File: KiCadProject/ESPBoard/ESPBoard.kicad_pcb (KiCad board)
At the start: 6 copper layers, 44.9 x 42.5 mm, 77 parts, among them J201 Conn_02x05, J202 Conn_01x02, J203 Conn_02x05, J204 JST_SM04B, J205 DNP, J206 1x05 female, J207 JST_SM04B, Q401 NFET_Gatenames, Q402 PMOS_Gatenames, Q403 NFET_Gatenames, Q404 PMOS_Gatenames, Q405 NFET_Gatenames, Q406 PMOS_Gatenames, Q407 NFET_Gatenames, Q408 PMOS_Gatenames, SW301 SW_Push, SW302 SW_Push, U301 ESP32-S3-WROOM-1

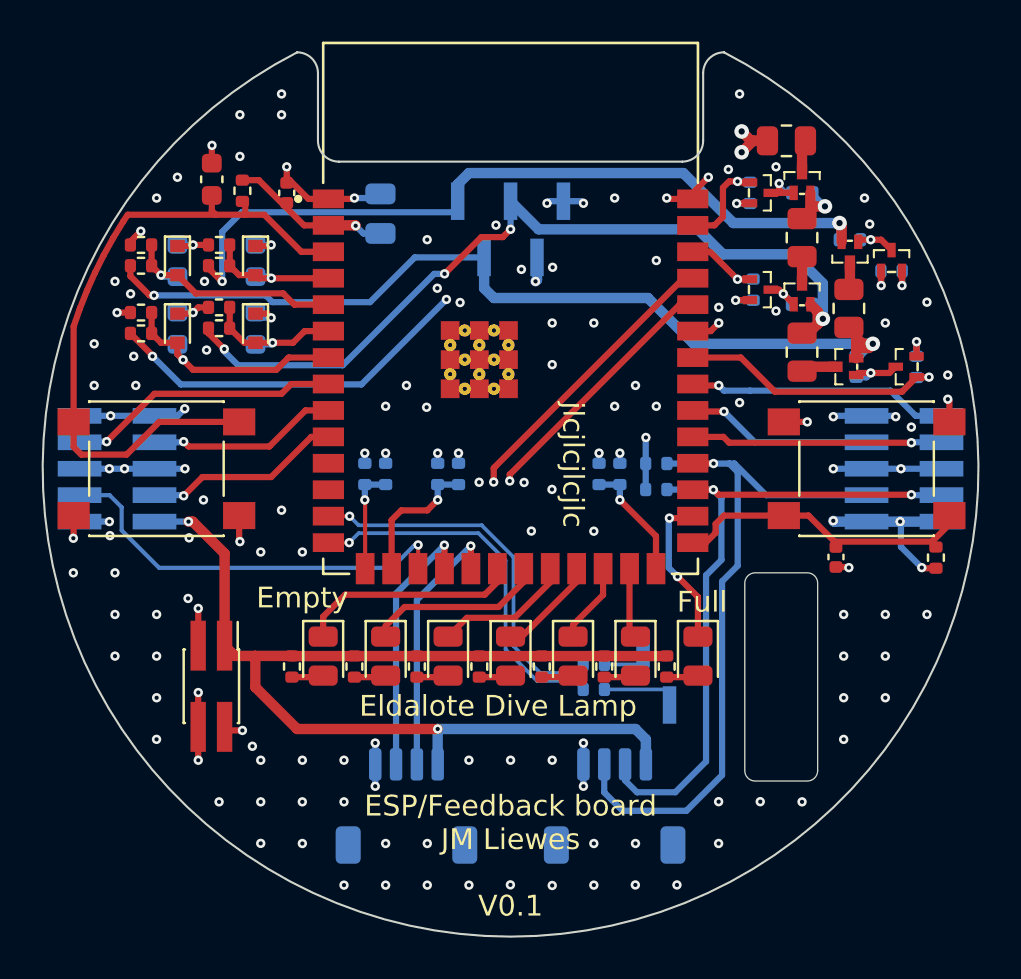
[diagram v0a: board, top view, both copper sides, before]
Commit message: Made ready to order PCBs. Some problems with ordering due to misunderstanding. Thinking about solutions
Signed-off-by: Eldalote.Electronics <Eldalote.Electronics@gmail.com>
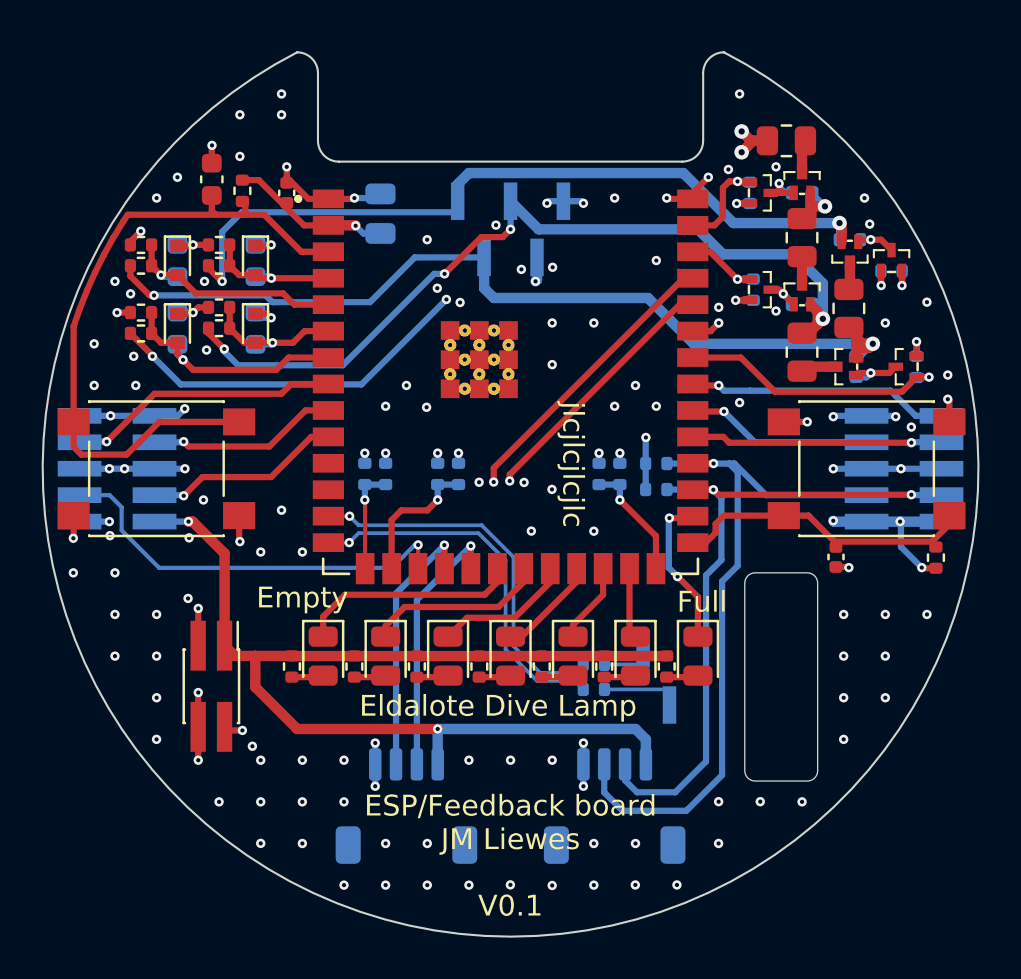
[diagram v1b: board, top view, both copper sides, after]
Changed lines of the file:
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@@
       (layerselection 0x00010fc_ffffffff)
       (disableapertmacros false)
-      (usegerberextensions false)
+      (usegerberextensions true)
       (usegerberattributes true)
       (usegerberadvancedattributes true)
@@
       (plotinvisibletext false)
       (sketchpadsonfab false)
-      (subtractmaskfromsilk false)
+      (subtractmaskfromsilk true)
       (outputformat 1)
       (mirror false)
-      (drillshape 1)
+      (drillshape 0)
       (scaleselection 1)
-      (outputdirectory "")
+      (outputdirectory "Fab/")
     )
   )
@@
     (fp_line (start -1 -0.625) (end 1 -0.625) (layer "F.Fab") (width 0.1))
     (fp_line (start 1 0.625) (end -1 0.625) (layer "F.Fab") (width 0.1))
-    (pad "1" smd roundrect (at -0.9125 0 270) (size 1.025 1.4) (layers "F.Cu" "F.Paste" "F.Mask") (roundrect_rratio 0.243902)
+    (pad "1" smd roundrect (at -0.9125 0 270) (size 1.025 1.4) (layers "F.Cu" "F.Paste" "F.Mask") (roundrect_rratio 0.243902439)
       (net 57 "/P4 Batsense-Balancing/C4L") (pintype "passive"))
-    (pad "2" smd roundrect (at 0.9125 0 270) (size 1.025 1.4) (layers "F.Cu" "F.Paste" "F.Mask") (roundrect_rratio 0.243902)
+    (pad "2" smd roundrect (at 0.9125 0 270) (size 1.025 1.4) (layers "F.Cu" "F.Paste" "F.Mask") (roundrect_rratio 0.243902439)
       (net 40 "Cell3") (pintype "passive"))
     (model "${KICAD6_3DMODEL_DIR}/Resistor_SMD.3dshapes/R_0805_2012Metric.wrl"
@@
     (fp_line (start 1 0.625) (end -1 0.625) (layer "F.Fab") (width 0.1))
     (fp_line (start -1 -0.625) (end 1 -0.625) (layer "F.Fab") (width 0.1))
-    (pad "1" smd roundrect (at -0.9125 0 90) (size 1.025 1.4) (layers "F.Cu" "F.Paste" "F.Mask") (roundrect_rratio 0.243902)
+    (pad "1" smd roundrect (at -0.9125 0 90) (size 1.025 1.4) (layers "F.Cu" "F.Paste" "F.Mask") (roundrect_rratio 0.243902439)
       (net 58 "/P4 Batsense-Balancing/C3L") (pintype "passive"))
-    (pad "2" smd roundrect (at 0.9125 0 90) (size 1.025 1.4) (layers "F.Cu" "F.Paste" "F.Mask") (roundrect_rratio 0.243902)
+    (pad "2" smd roundrect (at 0.9125 0 90) (size 1.025 1.4) (layers "F.Cu" "F.Paste" "F.Mask") (roundrect_rratio 0.243902439)
       (net 41 "Cell2") (pintype "passive"))
     (model "${KICAD6_3DMODEL_DIR}/Resistor_SMD.3dshapes/R_0805_2012Metric.wrl"
@@
       (effects (font (size 1 1) (thickness 0.15)))
     )
-    (fp_line (start -9 -12.75) (end 9 -12.75) (layer "F.SilkS") (width 0.127))
     (fp_line (start -9 12.02) (end -9 12.75) (layer "F.SilkS") (width 0.127))
-    (fp_line (start 9 -12.75) (end 9 -6.03) (layer "F.SilkS") (width 0.127))
     (fp_line (start 9 12.02) (end 9 12.75) (layer "F.SilkS") (width 0.127))
     (fp_line (start 9 12.75) (end 7.755 12.75) (layer "F.SilkS") (width 0.127))
     (fp_line (start -9 12.75) (end -7.755 12.75) (layer "F.SilkS") (width 0.127))
-    (fp_line (start -9 -6.03) (end -9 -12.75) (layer "F.SilkS") (width 0.127))
     (fp_circle (center -10.2 -5.26) (end -10.1 -5.26) (layer "F.SilkS") (width 0.2) (fill none))
     (fp_line (start -9.75 13.5) (end -9.75 -13) (layer "F.CrtYd") (width 0.05))
@@
     (fp_line (start 1 0.625) (end -1 0.625) (layer "F.Fab") (width 0.1))
     (fp_line (start -1 -0.625) (end 1 -0.625) (layer "F.Fab") (width 0.1))
-    (pad "1" smd roundrect (at -0.9125 0 180) (size 1.025 1.4) (layers "F.Cu" "F.Paste" "F.Mask") (roundrect_rratio 0.243902)
+    (pad "1" smd roundrect (at -0.9125 0 180) (size 1.025 1.4) (layers "F.Cu" "F.Paste" "F.Mask") (roundrect_rratio 0.243902439)
       (net 60 "/P4 Batsense-Balancing/C1L") (pintype "passive"))
-    (pad "2" smd roundrect (at 0.9125 0 180) (size 1.025 1.4) (layers "F.Cu" "F.Paste" "F.Mask") (roundrect_rratio 0.243902)
+    (pad "2" smd roundrect (at 0.9125 0 180) (size 1.025 1.4) (layers "F.Cu" "F.Paste" "F.Mask") (roundrect_rratio 0.243902439)
       (net 21 "GND") (pintype "passive"))
     (model "${KICAD6_3DMODEL_DIR}/Resistor_SMD.3dshapes/R_0805_2012Metric.wrl"
@@
     (fp_line (start 1 0.625) (end -1 0.625) (layer "F.Fab") (width 0.1))
     (fp_line (start -1 -0.625) (end 1 -0.625) (layer "F.Fab") (width 0.1))
-    (pad "1" smd roundrect (at -0.9125 0 90) (size 1.025 1.4) (layers "F.Cu" "F.Paste" "F.Mask") (roundrect_rratio 0.243902)
+    (pad "1" smd roundrect (at -0.9125 0 90) (size 1.025 1.4) (layers "F.Cu" "F.Paste" "F.Mask") (roundrect_rratio 0.243902439)
       (net 59 "/P4 Batsense-Balancing/C2L") (pintype "passive"))
-    (pad "2" smd roundrect (at 0.9125 0 90) (size 1.025 1.4) (layers "F.Cu" "F.Paste" "F.Mask") (roundrect_rratio 0.243902)
+    (pad "2" smd roundrect (at 0.9125 0 90) (size 1.025 1.4) (layers "F.Cu" "F.Paste" "F.Mask") (roundrect_rratio 0.243902439)
       (net 42 "Cell1") (pintype "passive"))
     (model "${KICAD6_3DMODEL_DIR}/Resistor_SMD.3dshapes/R_0805_2012Metric.wrl"
@@
     (pad "4" smd roundrect (at 1.5 2 180) (size 0.6 1.55) (layers "B.Cu" "B.Paste" "B.Mask") (roundrect_rratio 0.25)
       (net 21 "GND") (pinfunction "Pin_4") (pintype "passive"))
-    (pad "MP" smd roundrect (at -2.8 -1.875 180) (size 1.2 1.8) (layers "B.Cu" "B.Paste" "B.Mask") (roundrect_rratio 0.208333))
-    (pad "MP" smd roundrect (at 2.8 -1.875 180) (size 1.2 1.8) (layers "B.Cu" "B.Paste" "B.Mask") (roundrect_rratio 0.208333))
+    (pad "MP" smd roundrect (at -2.8 -1.875 180) (size 1.2 1.8) (layers "B.Cu" "B.Paste" "B.Mask") (roundrect_rratio 0.2083333333))
+    (pad "MP" smd roundrect (at 2.8 -1.875 180) (size 1.2 1.8) (layers "B.Cu" "B.Paste" "B.Mask") (roundrect_rratio 0.2083333333))
     (model "F:/Engineering/Projects/Divelamp/KiCadImports/3DModels/SM04B-SRSS-TB.STEP"
       (offset (xyz 0 1.25 -0.25))
@@
     (pad "4" smd roundrect (at 1.5 2 180) (size 0.6 1.55) (layers "B.Cu" "B.Paste" "B.Mask") (roundrect_rratio 0.25)
       (net 21 "GND") (pinfunction "Pin_4") (pintype "passive"))
-    (pad "MP" smd roundrect (at 2.8 -1.875 180) (size 1.2 1.8) (layers "B.Cu" "B.Paste" "B.Mask") (roundrect_rratio 0.208333))
-    (pad "MP" smd roundrect (at -2.8 -1.875 180) (size 1.2 1.8) (layers "B.Cu" "B.Paste" "B.Mask") (roundrect_rratio 0.208333))
+    (pad "MP" smd roundrect (at 2.8 -1.875 180) (size 1.2 1.8) (layers "B.Cu" "B.Paste" "B.Mask") (roundrect_rratio 0.2083333333))
+    (pad "MP" smd roundrect (at -2.8 -1.875 180) (size 1.2 1.8) (layers "B.Cu" "B.Paste" "B.Mask") (roundrect_rratio 0.2083333333))
     (model "F:/Engineering/Projects/Divelamp/KiCadImports/3DModels/SM04B-SRSS-TB.STEP"
       (offset (xyz 0 1.25 -0.25))

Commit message: Started work on body 3d work
Signed-off-by: Eldalote.Electronics <Eldalote.Electronics@gmail.com>
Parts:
- moved R307 5.50 mm to (149.5, 100.2)
- moved R317 5.50 mm to (148.5, 100.2)
- moved R306 4.80 mm to (152.3, 100.2)
- moved R316 4.80 mm to (151.3, 100.2)
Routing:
- net +3V3: track 136.3 -> 127.7 mm, vias 11 -> 6
- net /P3 ESP32/Select 3: track 5.05 -> 9.25 mm
- net /P3 ESP32/Select 2: track 6.69 -> 10.8 mm
- net Cell1: track 42.8 -> 39.8 mm, vias 4 -> 5
- net UART_TXDO: track 35.2 -> 33.8 mm
- net UART_RXDO: track 36.2 -> 35.2 mm, vias 2 -> 4
- net I2C_SCL: track 35.3 -> 36.0 mm, vias 1 -> 2
- net GND: vias 143 -> 139
- added copper zone on In2.Cu, net GND
- removed copper zone on In3.Cu, net GND
- removed copper zone on In4.Cu, net GND
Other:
- copper layers 6 -> 4
